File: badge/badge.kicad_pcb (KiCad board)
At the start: 2 copper layers, 50.2 x 50.2 mm, 18 parts, among them J1 Conn_02x03_Odd_Even, U1 ATtiny424-SSU

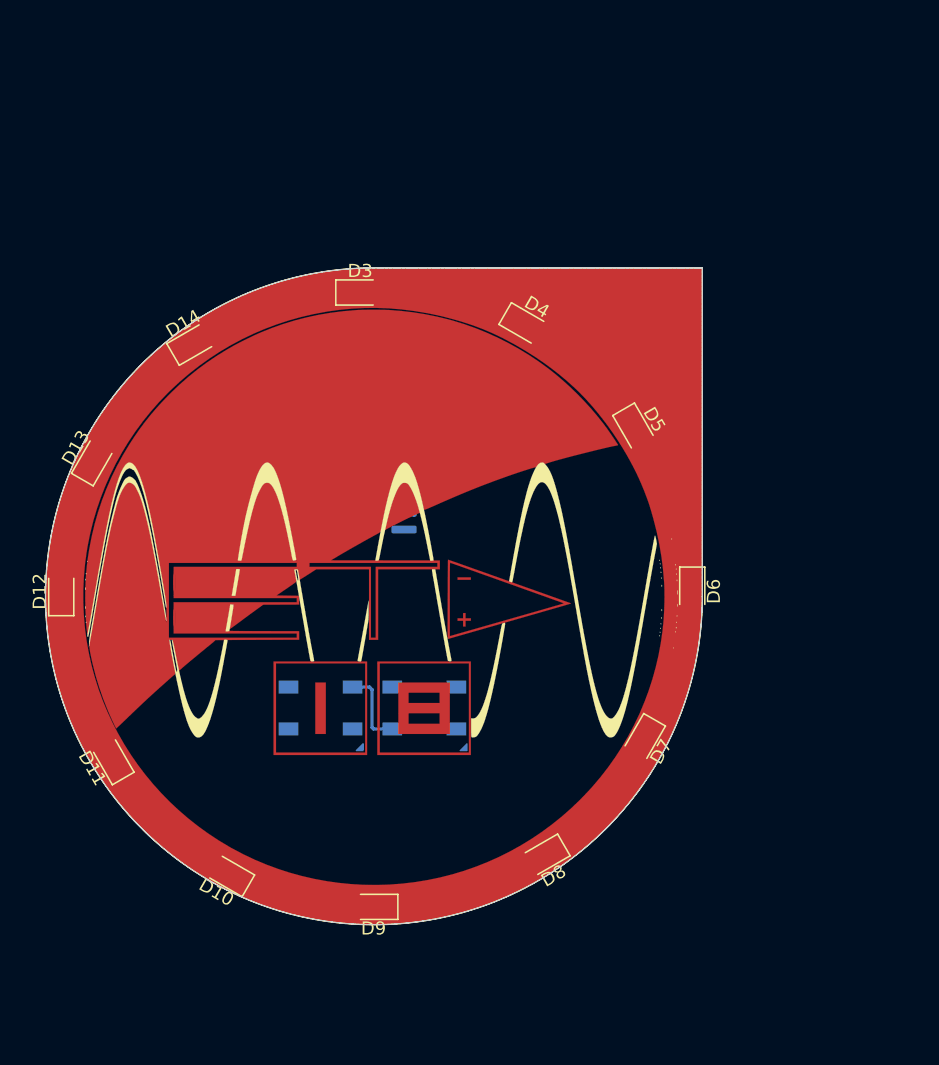
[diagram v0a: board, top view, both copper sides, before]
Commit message: schematic nearlly finished + new design on inkscape
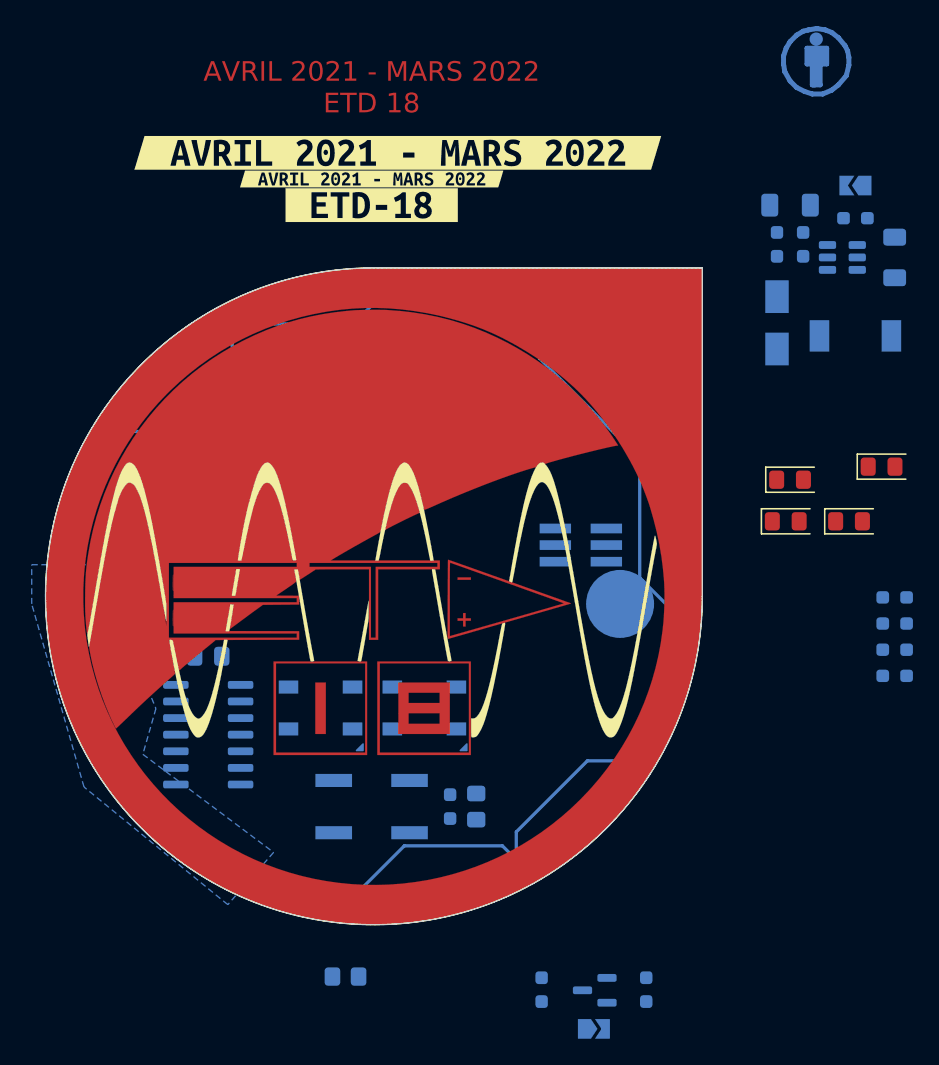
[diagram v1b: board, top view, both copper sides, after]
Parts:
- added BT1: Battery_Cell, badge:cr_2032_holder_S8421-45R, B.Cu at (199.0, 115.0)
- added C2: 22u, Resistor_SMD:R_1206_3216Metric_Pad1.30x1.75mm_HandSolder, B.Cu at (239.0, 104.0)
- added C3: 22u, Resistor_SMD:R_1206_3216Metric_Pad1.30x1.75mm_HandSolder, B.Cu at (231.0, 100.0)
- added C4: 100n, Resistor_SMD:R_0805_2012Metric_Pad1.20x1.40mm_HandSolder, B.Cu at (197.0, 159.0)
- added C5: 100n, Resistor_SMD:R_0805_2012Metric_Pad1.20x1.40mm_HandSolder, B.Cu at (207.0, 146.0)
- added D15: D_Schottky, Diode_SMD:D_SMA, B.Cu at (230.0, 109.0)
- added D16: LED, badge:LED_0805_2012_badge, F.Cu at (231.0, 121.0)
- added D17: LED, badge:LED_0805_2012_badge, F.Cu at (230.7, 124.2)
- added D18: LED, badge:LED_0805_2012_badge, F.Cu at (238.0, 120.0)
- added D19: LED, badge:LED_0805_2012_badge, F.Cu at (235.5, 124.2)
- added G1: KiCAD LOGO Small, Symbol:Symbol_CC-Attribution_CopperTop_Small, B.Cu at (233.0, 89.0)
- added H1: Badge Pin Pad, badge:pin_badge, B.Cu at (218.0, 130.5)
- added H2: Badge Pin Pad, badge:pin_badge, B.Cu at (180.5, 130.5)
- added JP1: SolderJumper_2_Open, Jumper:SolderJumper-2_P1.3mm_Open_TrianglePad1.0x1.5mm, B.Cu at (236.0, 98.5)
- added JP2: SolderJumper_2_Open, Jumper:SolderJumper-2_P1.3mm_Open_TrianglePad1.0x1.5mm, B.Cu at (216.0, 163.0)
- added L1: 33u, Inductor_SMD:L_6.3x6.3_H3, B.Cu at (236.0, 110.0)
- added Q1: BSS83P, Package_TO_SOT_SMD:SOT-23, B.Cu at (216.1, 160.1)
- added R1: 1k, Resistor_SMD:R_0603_1608Metric_Pad0.98x0.95mm_HandSolder, B.Cu at (239.0, 136.0)
- added R10: 10k, Resistor_SMD:R_0603_1608Metric_Pad0.98x0.95mm_HandSolder, B.Cu at (205.0, 146.0)
- added R2: 1k, Resistor_SMD:R_0603_1608Metric_Pad0.98x0.95mm_HandSolder, B.Cu at (239.0, 134.0)
- added R3: 1k, Resistor_SMD:R_0603_1608Metric_Pad0.98x0.95mm_HandSolder, B.Cu at (239.0, 132.0)
- added R4: 1k, Resistor_SMD:R_0603_1608Metric_Pad0.98x0.95mm_HandSolder, B.Cu at (239.0, 130.0)
- added R5: 75k, Resistor_SMD:R_0603_1608Metric_Pad0.98x0.95mm_HandSolder, B.Cu at (230.0, 103.0)
- added R6: 10k, Resistor_SMD:R_0603_1608Metric_Pad0.98x0.95mm_HandSolder, B.Cu at (232.0, 103.0)
- added R7: 10k, Resistor_SMD:R_0603_1608Metric_Pad0.98x0.95mm_HandSolder, B.Cu at (212.0, 160.0)
- added R8: 10k, Resistor_SMD:R_0603_1608Metric_Pad0.98x0.95mm_HandSolder, B.Cu at (220.0, 160.0)
- added R9: 10k, Resistor_SMD:R_0603_1608Metric_Pad0.98x0.95mm_HandSolder, B.Cu at (236.0, 101.0)
- added SW1: SK-3296S-01-L1, badge:sk-3296s-01-l1, B.Cu at (222.4, 109.5)
- added SW2: SW_Push, Button_Switch_SMD:SW_Push_1P1T_NO_CK_KSC6xxJ, B.Cu at (199.0, 146.0)
- added U2: MT3608, Package_TO_SOT_SMD:SOT-23-6, B.Cu at (235.0, 104.0)
- added kibuzzard-635F9BF9: G***, kibuzzard-635F9BF9, F.Cu at (199.0, 100.0)
- added kibuzzard-635F9CA7: G***, kibuzzard-635F9CA7, F.Cu at (201.0, 96.0)
- added kibuzzard-635F9CB1: G***, kibuzzard-635F9CB1, F.Cu at (199.0, 98.0)
- D10, D11, D12, D13, D14, D3, D4, D5, D6, D7, D8, D9: footprint LED_SMD:LED_0805_2012Metric_Pad1.15x1.40mm_HandSolder -> badge:LED_0805_2012_badge; moved to B.Cu
- moved D6 47.8 mm to (175.7, 129.9)
- moved D12 47.4 mm to (222.7, 129.9)
- moved D13 41.8 mm to (219.6, 118.2), turned to 120 degrees
- moved D7 40.9 mm to (178.8, 141.7), turned to -60 degrees
- moved D11 40.5 mm to (219.6, 141.7), turned to 60 degrees
- moved D5 40.4 mm to (178.8, 118.2), turned to -120 degrees
- moved D14 25.5 mm to (210.9, 109.6), turned to 150 degrees
- moved D8 24.6 mm to (187.4, 150.3), turned to -30 degrees
- moved C1 23.8 mm to (186.5, 134.5), turned to 180 degrees
- moved D4 23.4 mm to (187.4, 109.6), turned to -150 degrees
- moved U1 23.2 mm to (186.5, 140.5)
- moved D10 23.0 mm to (210.9, 150.3), turned to 30 degrees
- moved J1 20.6 mm to (215.0, 126.0)
- moved D3 1.10 mm to (199.2, 106.5), turned to 180 degrees
- moved D9 0.23 mm to (199.2, 153.4), turned to 0 degrees
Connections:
- net /UDPI renamed /ROW0
- net Net-(D1-Pad2) renamed /NEO_2
- D1 pad 1: VCC -> +5V
- D1 pad 4: unconnected-(D1-Pad4) -> /NEO_1
- D10 pad 1: unconnected-(D10-Pad1) -> /COL2
- D10 pad 2: unconnected-(D10-Pad2) -> Net-(D10-Pad2)
- D11 pad 1: unconnected-(D11-Pad1) -> /COL2
- D11 pad 2: unconnected-(D11-Pad2) -> Net-(D11-Pad2)
- D12 pad 1: unconnected-(D12-Pad1) -> /COL3
- D12 pad 2: unconnected-(D12-Pad2) -> Net-(D12-Pad2)
- D13 pad 1: unconnected-(D13-Pad1) -> /COL3
- D13 pad 2: unconnected-(D13-Pad2) -> Net-(D10-Pad2)
- D14 pad 1: unconnected-(D14-Pad1) -> /COL3
- D14 pad 2: unconnected-(D14-Pad2) -> Net-(D11-Pad2)
- D2 pad 1: VCC -> +5V
- D3 pad 1: unconnected-(D3-Pad1) -> /COL0
- D3 pad 2: unconnected-(D3-Pad2) -> Net-(D12-Pad2)
- D4 pad 1: unconnected-(D4-Pad1) -> /COL0
- D4 pad 2: unconnected-(D4-Pad2) -> Net-(D10-Pad2)
- D5 pad 1: unconnected-(D5-Pad1) -> /COL0
- D5 pad 2: unconnected-(D5-Pad2) -> Net-(D11-Pad2)
- D6 pad 1: unconnected-(D6-Pad1) -> /COL1
- D6 pad 2: unconnected-(D6-Pad2) -> Net-(D12-Pad2)
- D7 pad 1: unconnected-(D7-Pad1) -> /COL1
- D7 pad 2: unconnected-(D7-Pad2) -> Net-(D10-Pad2)
- D8 pad 1: unconnected-(D8-Pad1) -> /COL1
- D8 pad 2: unconnected-(D8-Pad2) -> Net-(D11-Pad2)
- D9 pad 1: unconnected-(D9-Pad1) -> /COL2
- D9 pad 2: unconnected-(D9-Pad2) -> Net-(D12-Pad2)
- U1 pad 11: unconnected-(U1-Pad11) -> /ROW1
- U1 pad 12: unconnected-(U1-Pad12) -> /ROW2
- U1 pad 13: unconnected-(U1-Pad13) -> /ROW3
- U1 pad 2: unconnected-(U1-Pad2) -> /COL0
- U1 pad 3: unconnected-(U1-Pad3) -> /COL1
- U1 pad 4: unconnected-(U1-Pad4) -> /COL2
- U1 pad 5: unconnected-(U1-Pad5) -> /COL3
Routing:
- net /COL2: track 0.00 -> 29.7 mm
- net /COL3: track 0.00 -> 26.8 mm
- net /COL0: track 0.00 -> 26.6 mm
- net /ROW0: track 12.1 -> 0.00 mm
- net /NEO_2: track 6.06 -> 0.00 mm
- added copper zone on B.Cu, net /COL1
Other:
- board text added: "AVRIL 2021 - MARS 2022 ETD 18"
